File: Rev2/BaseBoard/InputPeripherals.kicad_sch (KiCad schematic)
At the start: 19 parts, among them J3 Conn_01x03_Socket, J4 SJ1-3523N, U4 LF353N, U5 LF353N, U6 MCP3202

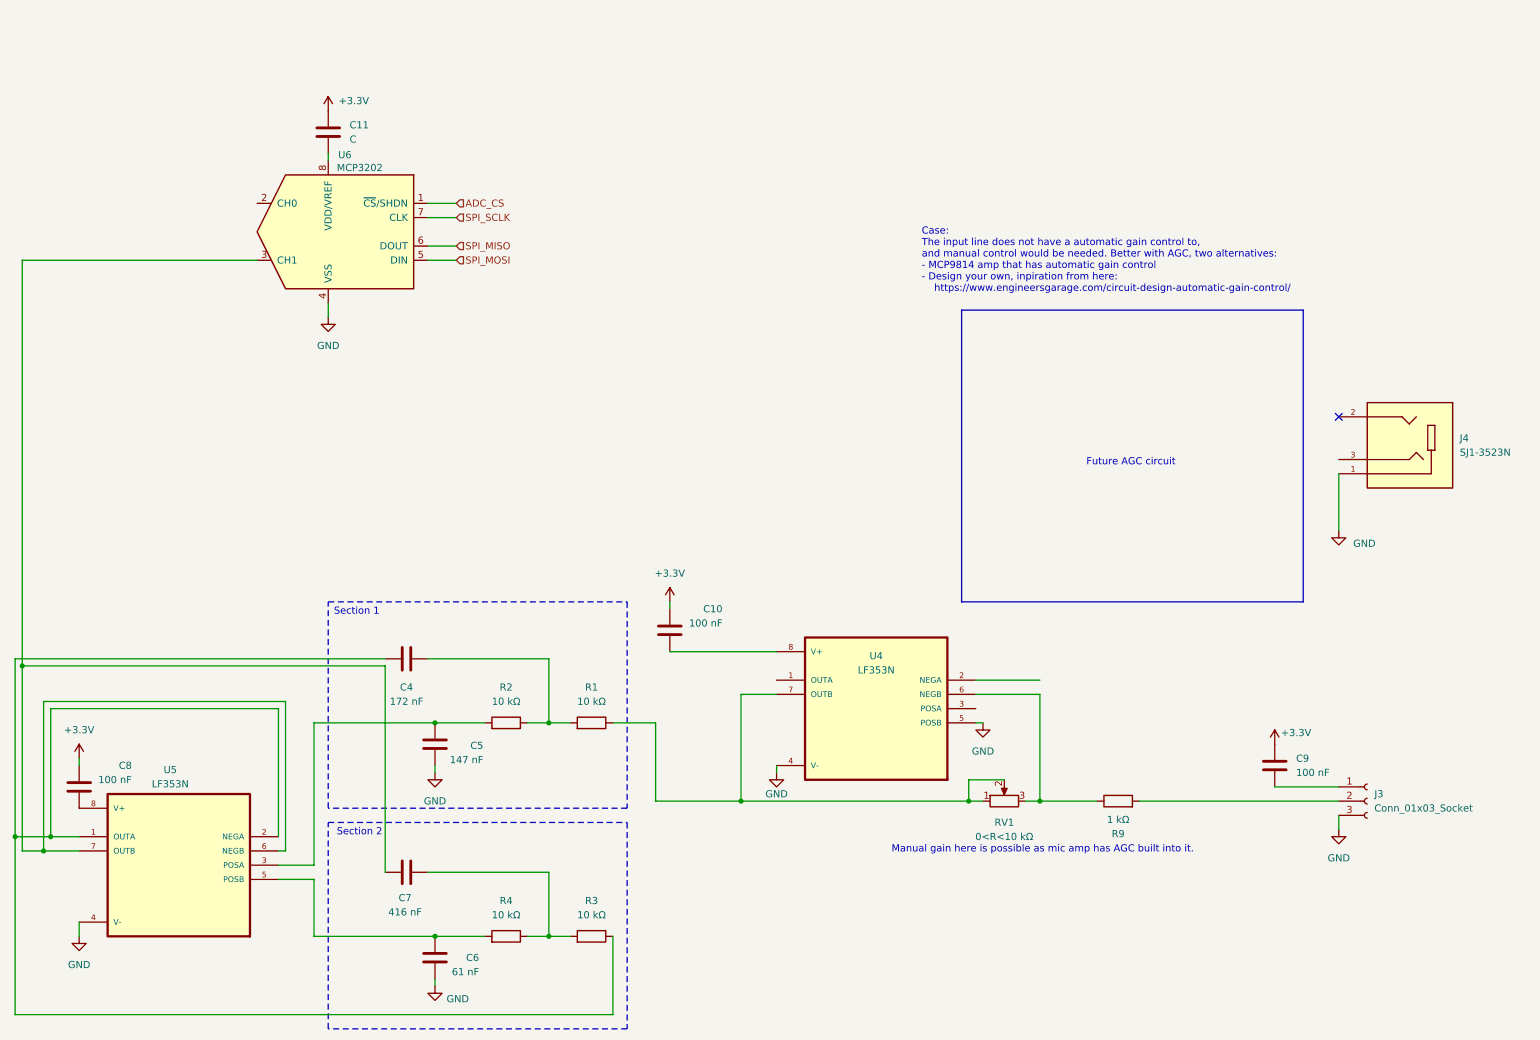
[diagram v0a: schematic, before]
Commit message: Added Testpoints, UART and JTAG
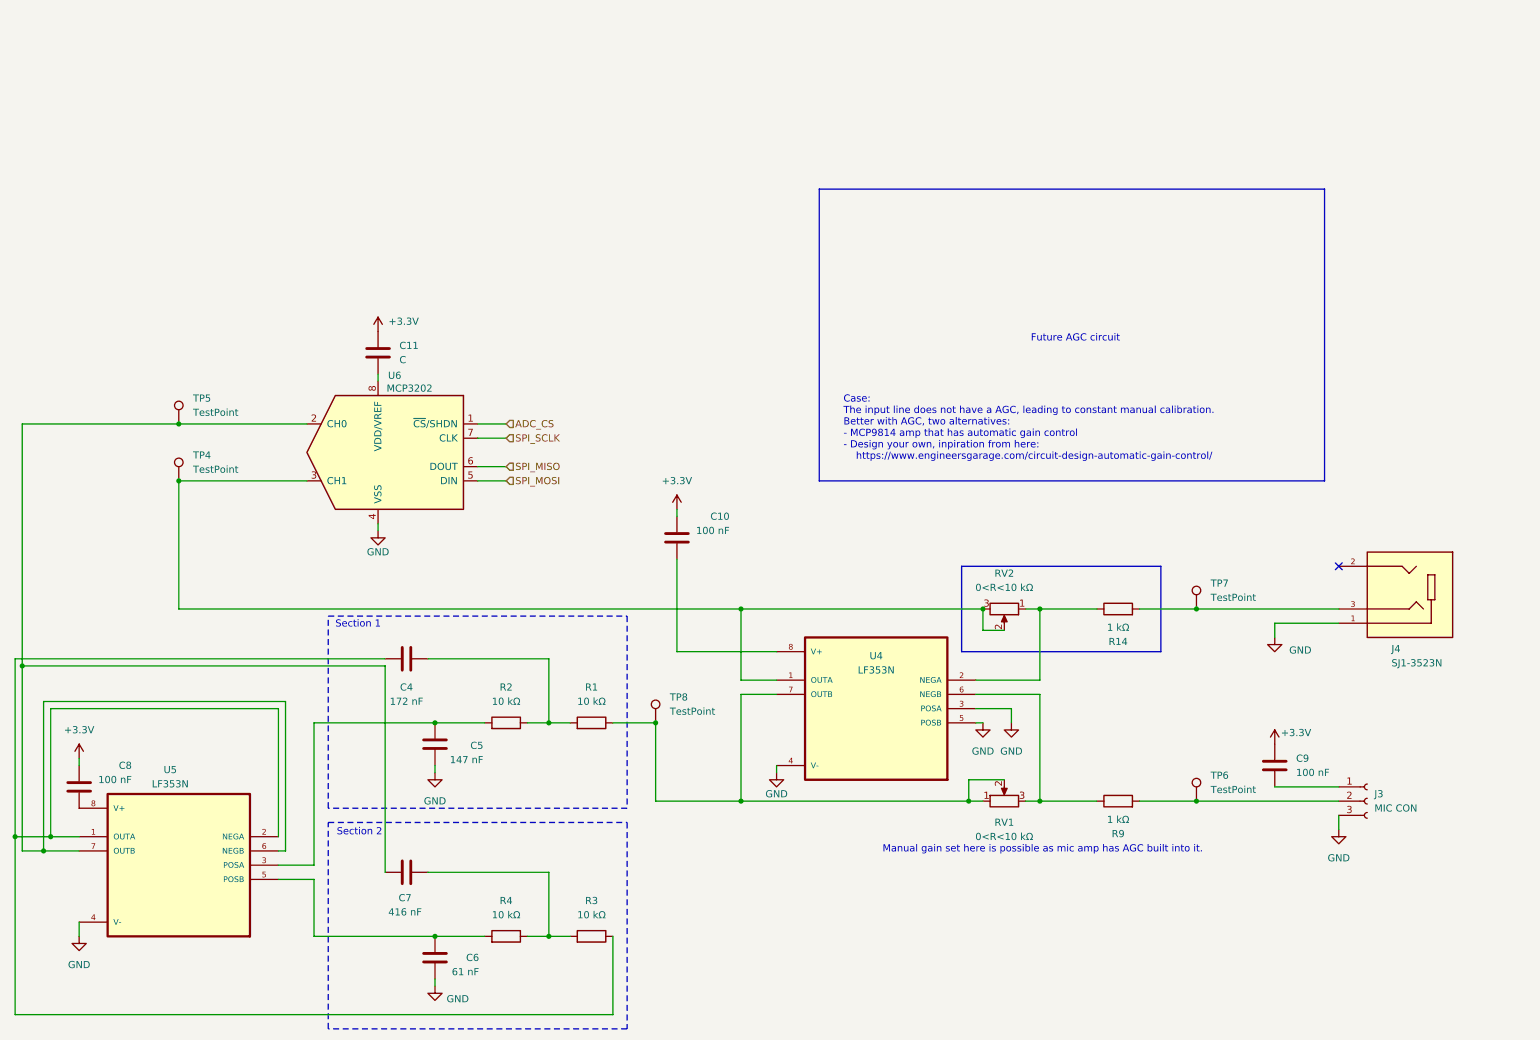
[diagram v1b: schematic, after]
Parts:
- added R14: 1 kΩ, symbol Device:R
- added RV2: 0<R<10 kΩ, symbol Device:R_Potentiometer
- added TP4, TP5, TP6, TP7, TP8: TestPoint, symbol Connector:TestPoint
- J3: value Conn_01x03_Socket -> MIC CON
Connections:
- net GND: now also U4.3 (POSA)
- net at U6.2 (CH0): now also C7.2, U5.6 (NEGB), U5.7 (OUTB), TP5.1
- net at J3.2 (Pin_2), R9.2: now also TP6.1
- net at U4.1 (OUTA): now also U6.3 (CH1), RV2.2, RV2.3, TP4.1
- net at U4.2 (NEGA): now also R14.1, RV2.1
- net at R1.1, RV1.1, RV1.2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: now also TP8.1
- net at J4.3: now also R14.2, TP7.1
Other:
- note added: "Case: The input line does not have a AGC, leading to constant manual calibration. Better with AGC, two alternatives: - MCP9814 amp that has automatic gain control - Design your own, inpiration from here: https://www.engineersgarage.com/circuit-design-automatic-gain-control/"
- note added: "Manual gain set here is possible as mic amp has AGC built into it."
- note removed: "Case: The input line does not have a automatic gain control to, and manual control would be needed. Better with AGC, two alternatives: - MCP9814 amp that has automatic gain control - Design your own, inpiration from here: https://www.engineersgarage.com/circuit-design-automatic-gain-control/"
- note removed: "Manual gain here is possible as mic amp has AGC built into it."
- moved on the sheet: C10, C11, J4, U6

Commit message: Finished placement, routing remains
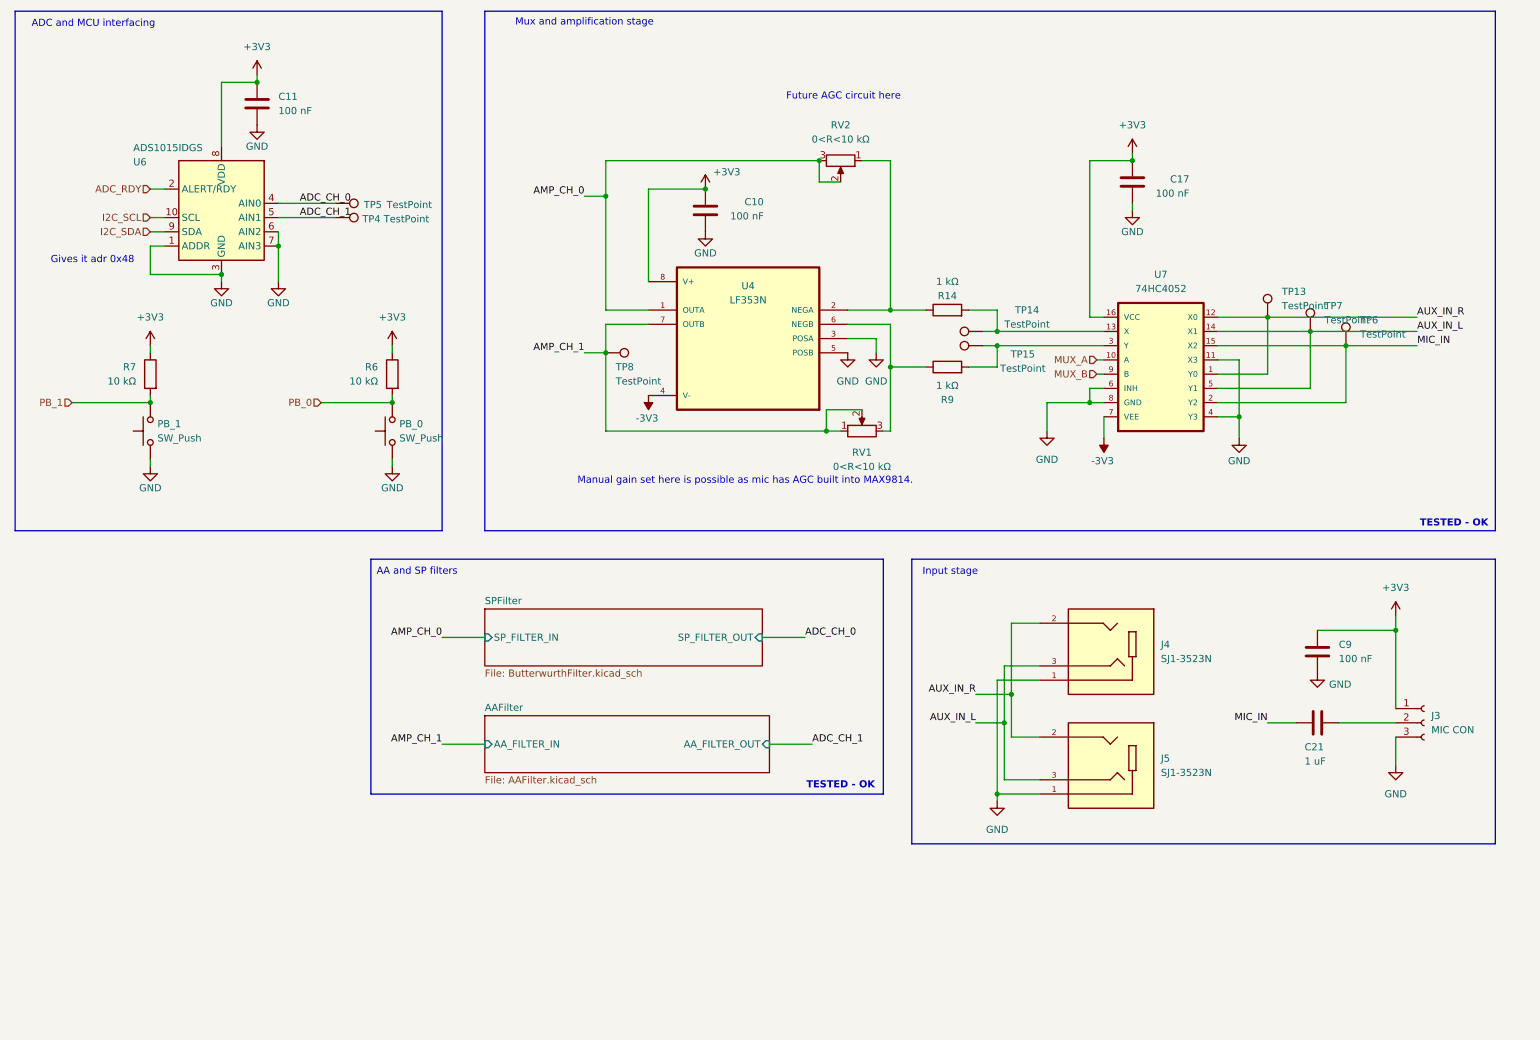
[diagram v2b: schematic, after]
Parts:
- removed C4: 172 nF, symbol Device:C
- removed C5: 147 nF, symbol Device:C
- removed C6: 61 nF, symbol Device:C
- removed C7: 416 nF, symbol Device:C
- removed C8: 100 nF, symbol Device:C
- removed R1, R2, R3, R4: 10 kΩ, symbol Device:R
- removed U5: LF353N, LF353N:DIP794W45P254L959H508Q8, symbol LF353N:LF353N
- removed U6: MCP3202, symbol Analog_ADC:MCP3202
- added C17: 100 nF, Capacitor_SMD:C_0805_2012Metric_Pad1.18x1.45mm_HandSolder, symbol Device:C
- added C21: 1 uF, Capacitor_SMD:C_0805_2012Metric_Pad1.18x1.45mm_HandSolder, symbol Device:C
- added J5: SJ1-3523N, Symbols:CUI_SJ1-3523N, symbol SJ1-3523N:SJ1-3523N
- added PB_0, PB_1: SW_Push, Button_Switch_SMD:SW_Push_1P1T_NO_6x6mm_H9.5mm, symbol Switch:SW_Push
- added R6, R7: 10 kΩ, Resistor_SMD:R_0805_2012Metric_Pad1.20x1.40mm_HandSolder, symbol Device:R
- added TP13, TP14, TP15: TestPoint, TestPoint:TestPoint_Pad_1.0x1.0mm, symbol Connector:TestPoint
- added U6: ADS1015IDGS, Package_SO:TSSOP-10_3x3mm_P0.5mm, symbol Analog_ADC:ADS1015IDGS
- added U7: 74HC4052, USR_LIB:MUX, symbol 74HC4052:74HC4052
- C10, C9: footprint (none) -> Capacitor_SMD:C_0805_2012Metric_Pad1.18x1.45mm_HandSolder
- C11: value C -> 100 nF; footprint (none) -> Capacitor_SMD:C_0805_2012Metric_Pad1.18x1.45mm_HandSolder
- J4: footprint SJ1-3523N:CUI_SJ1-3523N -> Symbols:CUI_SJ1-3523N
- R14, R9: footprint (none) -> Resistor_SMD:R_0805_2012Metric_Pad1.20x1.40mm_HandSolder
- RV1, RV2: footprint (none) -> Connector_PinSocket_2.54mm:PinSocket_1x03_P2.54mm_Vertical
- TP4, TP5, TP6, TP7, TP8: footprint (none) -> TestPoint:TestPoint_Pad_1.0x1.0mm
- U4: footprint LF353N:DIP794W45P254L959H508Q8 -> USR_LIB:LF353
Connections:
- net +3.3V is gone; now on net +3V3: C10.1, C11.1, C9.1
- net GND: now also C10.2, C11.2, C9.2, C17.2, J5.1, PB_0.2, PB_1.2, U6.1 (ADDR), U6.3 (GND), U6.6 (AIN2), U6.7 (AIN3), U7.11 (X3), U7.4 (Y3), U7.6 (INH), U7.8 (GND); no longer U4.4 (V-)
- net ADC_CH_0: now reaches TP5.1
- net ADC_CH_0: now also U6.4 (AIN0)
- net AMP_CH_0: now reaches RV2.2, RV2.3, U4.1 (OUTA)
- net AMP_CH_0: no longer TP4.1
- net +3V3: now reaches U4.8 (V+)
- net +3V3: now also J3.1 (Pin_1), C17.1, R6.1, R7.1, U6.8 (VDD), U7.16 (VCC); no longer C10.2
- net AMP_CH_1: now reaches RV1.1, RV1.2, TP8.1, U4.7 (OUTB)
- net AUX_IN_L: now reaches J4.3, TP7.1
- net AUX_IN_L: now also J5.3, U7.14 (X1), U7.5 (Y1); no longer R14.2
- net AUX_IN_R: now reaches J4.2
- net AUX_IN_R: now also J5.2, TP13.1, U7.1 (Y0), U7.12 (X0)
- new net: R14.2, TP14.1, U7.13 (X)
- new net: R9.2, TP15.1, U7.3 (Y)
- new net: C21.1, J3.2 (Pin_2)
- new net -3V3: U4.4 (V-), U7.7 (VEE)
- new net ADC_CH_1: TP4.1, U6.5 (AIN1)
- new net ADC_RDY: U6.2 (ALERT/RDY)
- new net I2C_SCL: U6.10 (SCL)
- new net I2C_SDA: U6.9 (SDA)
- new net MIC_IN: C21.2, TP6.1, U7.15 (X2), U7.2 (Y2)
- new net MUX_A: U7.10 (A)
- new net MUX_B: U7.9 (B)
- new net PB_0: PB_0.1, R6.2
- new net PB_1: PB_1.1, R7.2
- no-connect marks 1 -> 0
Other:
- added sheet AAFilter (AAFilter.kicad_sch)
- added sheet SPFilter (ButterwurthFilter.kicad_sch)
- note added: "AA and SP filters"
- note added: "ADC and MCU interfacing"
- note added: "Future AGC circuit here"
- note added: "Gives it adr 0x48"
- note added: "Input stage"
- note added: "Manual gain set here is possible as mic has AGC built into MAX9814."
- note added: "Mux and amplification stage"
- note added: "TESTED - OK"
- note removed: "Case: The input line does not have a AGC, leading to constant manual calibration. Better with AGC, two alternatives: - MCP9814 amp that has automatic gain control - Design your own, inpiration from here: https://www.engineersgarage.com/circuit-design-automatic-gain-control/"
- note removed: "Future AGC circuit"
- note removed: "Manual gain set here is possible as mic amp has AGC built into it."
- note removed: "Section 1"
- note removed: "Section 2"
- moved on the sheet: C10, C11, R14, R9, RV1, RV2, TP4, TP5, TP8, U4

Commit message: Finished rev 2
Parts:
- renumbered PB_0 to PB0, PB_1 to PB1
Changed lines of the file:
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@@
 		(dnp no)
 		(fields_autoplaced yes)
-		(property "Reference" "PB_1"
+		(property "Reference" "PB1"
 			(at 41.91 86.3599 90)
 			(effects
@@
 			(project "BaseBoard"
 				(path "/5772fade-5f5a-4b33-b088-e12fff8be0e3/5c7a8f5b-ceaf-4fe8-9c69-7311132cd264"
-					(reference "PB_1")
+					(reference "PB1")
 					(unit 1)
 				)
@@
 		(dnp no)
 		(fields_autoplaced yes)
-		(property "Reference" "PB_0"
+		(property "Reference" "PB0"
 			(at 85.09 86.3599 90)
 			(effects
@@
 			(project ""
 				(path "/5772fade-5f5a-4b33-b088-e12fff8be0e3/5c7a8f5b-ceaf-4fe8-9c69-7311132cd264"
-					(reference "PB_0")
-					(unit 1)
-				)
+					(reference "PB0")
+					(unit 1)
+				)
